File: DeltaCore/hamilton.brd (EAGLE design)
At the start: 45 x 41 mm, 68 parts, among them Q3 MOSFET-NCHANNEL_SOT23-3, Q4 MOSFET-NCHANNEL_SOT23-3, Q5 MOSFET-NCHANNEL_SOT23-3, Q6 MOSFET-NCHANNEL_SOT23-3, Q7 NFET_AON7408, Q8 NFET_AON7408, U1 SAMR21, U10 PCA9557, U2 APDS9007, U3 MMA7660FC, U4 AT30TS74, U5 MCP73871-2AAI/ML, U7 BQ29718, U8 MCP1824ST-3302E/DB, U9 TPS61090, X1 XTAL

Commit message: more
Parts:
- removed R3: 20k, storm:S0402
- removed U2: APDS9007, storm:APDS9007
- moved R14 1.16 mm to (26.7, 36.7), turned to 0 degrees
- moved C12 0.77 mm to (43.8, 18.9)
- moved R12 0.61 mm to (23.0, 39.0)
- moved C13 0.13 mm to (35.2, 39.7)
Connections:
- net +3V3: no longer U2.4, U5.17, U5.3, U5.4, U5.9
- net GND: no longer R3.P$1, U2.1
- net LS: no longer R3.P$2, U2.3
- net SD: no longer U2.6
- net VCC: now also U5.17, U5.3, U5.4, U5.9
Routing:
- net VCC: track 17.8 -> 41.8 mm, vias 0 -> 3
- net LS: track 22.3 -> 0.00 mm, vias 2 -> 0
- net +3V3: track 68.4 -> 52.8 mm, vias 13 -> 8
- net SD: track 13.9 -> 0.00 mm
- net SCL: track 52.8 -> 42.6 mm, vias 4 -> 2
- net GND: track 219.0 -> 209.5 mm, vias 60 -> 59
- net OUT: track 81.8 -> 83.6 mm
- net SDA: track 45.9 -> 47.5 mm
- net ACC: track 12.1 -> 10.8 mm, vias 1 -> 0
- net !RESET!: track 16.5 -> 17.8 mm
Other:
- board size 45 x 41 mm -> 45 x 41.5 mm

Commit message: add analog line for fan
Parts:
- added JP9: (no value), pinhead:1X01
- added R16: 5k, resistor:R0402
- added R3: 20k, resistor:R0402
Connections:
- new net N$8: JP9.1, R3.2
- new net N$9: R16.2, R3.1, U1.8
- net GND: now also R16.1
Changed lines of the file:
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@@
 <element name="R4" library="resistor" package="R0603" value="??" x="5.842" y="3.556" rot="R90"/>
 <element name="R15" library="resistor" package="R0603" value="??" x="8.382" y="3.556" rot="R270"/>
+<element name="JP9" library="pinhead" package="1X01" value="" x="7.112" y="10.922"/>
+<element name="R3" library="resistor" package="R0402" value="20k" x="0.254" y="-4.318"/>
+<element name="R16" library="resistor" package="R0402" value="5k" x="0.254" y="-7.874"/>
 </elements>
 <signals>
@@
 <wire x1="36.867" y1="30.912" x2="36.728" y2="31.051" width="0.1524" layer="1"/>
 <wire x1="36.728" y1="31.051" x2="36.347" y2="31.051" width="0.1524" layer="1"/>
+<contactref element="R16" pad="1"/>
+<wire x1="2.27" y1="4.556" x2="-0.396" y2="-7.874" width="0" layer="19" extent="1-1"/>
 </signal>
 <signal name="N$3">
@@
 <wire x1="41.159" y1="20.764" x2="39.8912" y2="20.764" width="0.1524" layer="1"/>
 <wire x1="36.708" y1="26.499" x2="36.708" y2="27.762" width="0.1524" layer="1"/>
-<wire x1="36.708" y1="26.499" x2="37.0078" y2="26.1992" width="0.1524" layer="1"/>
-<wire x1="37.0078" y1="26.1992" x2="37.0078" y2="22.4028" width="0.1524" layer="1"/>
+<wire x1="36.708" y1="26.499" x2="37.0078" y2="25.9452" width="0.1524" layer="1"/>
+<wire x1="37.0078" y1="25.9452" x2="37.0078" y2="22.4028" width="0.1524" layer="1"/>
 <wire x1="37.0078" y1="22.4028" x2="37.846" y2="22.4028" width="0.1524" layer="1"/>
 <wire x1="37.8714" y1="21.59" x2="39.1668" y2="21.59" width="0.1524" layer="1"/>
@@
 <wire x1="6.858" y1="8.116" x2="10.8864" y2="8.116" width="0.3048" layer="1"/>
 </signal>
+<signal name="N$8">
+<contactref element="JP9" pad="1"/>
+<contactref element="R3" pad="2"/>
+<wire x1="0.904" y1="-4.318" x2="7.112" y2="10.922" width="0" layer="19" extent="1-1"/>
+</signal>
+<signal name="N$9">
+<contactref element="R3" pad="1"/>
+<contactref element="R16" pad="2"/>
+<contactref element="U1" pad="8"/>
+<wire x1="-0.396" y1="-4.318" x2="37.208" y2="27.762" width="0" layer="19" extent="1-1"/>
+<wire x1="0.904" y1="-7.874" x2="-0.396" y2="-4.318" width="0" layer="19" extent="1-1"/>
+</signal>
 </signals>

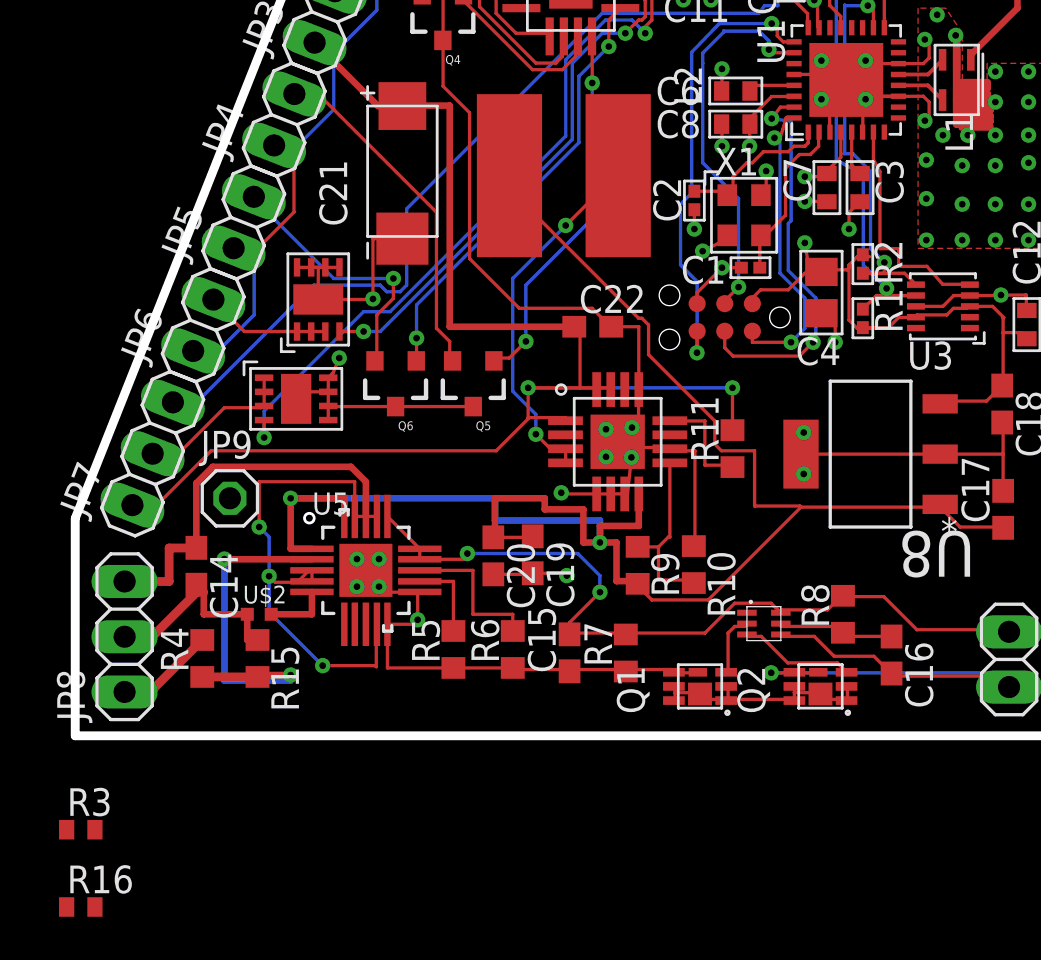
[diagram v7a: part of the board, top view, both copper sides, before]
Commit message: place resistors
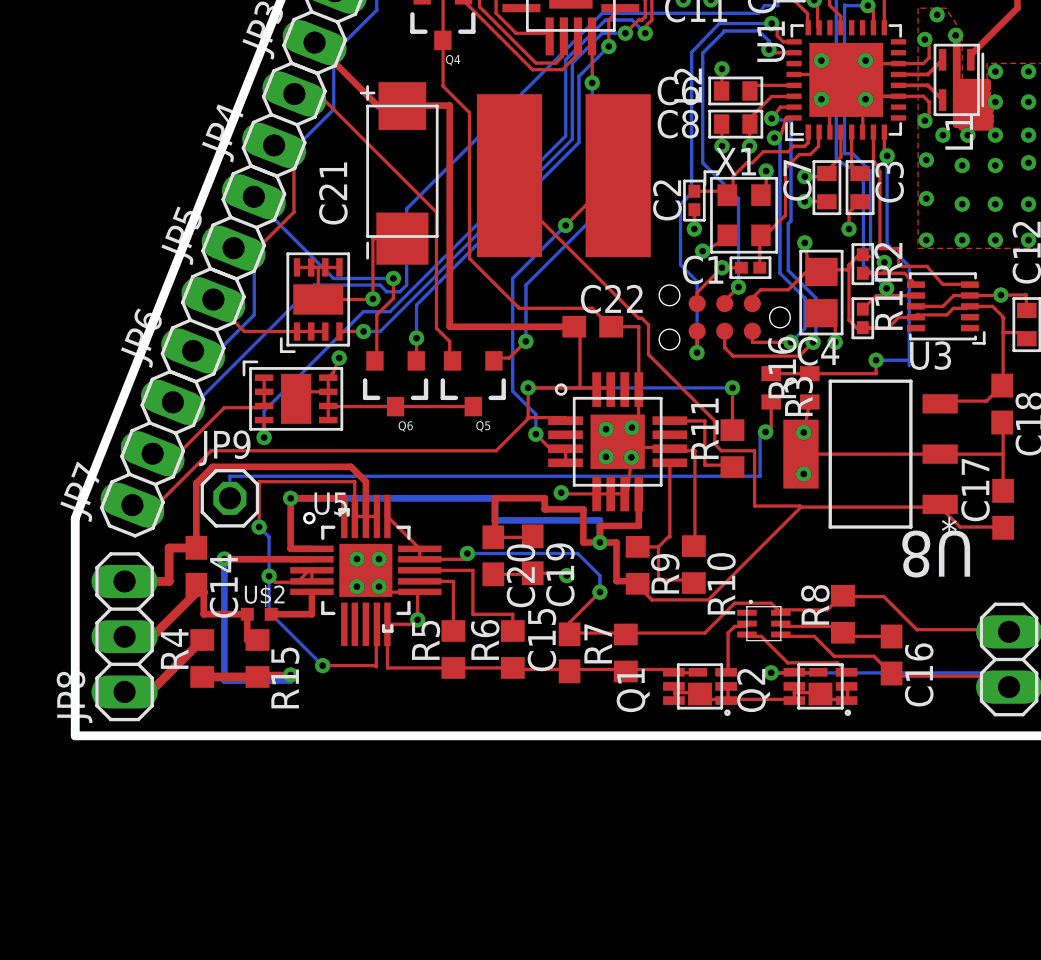
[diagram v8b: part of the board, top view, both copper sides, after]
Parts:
- moved R16 41.2 mm to (33.8, 16.0), turned to 90 degrees
- moved R3 37.7 mm to (32.0, 16.0), turned to 270 degrees
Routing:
- net N$8: track 0.00 -> 29.3 mm, vias 0 -> 1
- net N$9: track 0.00 -> 18.2 mm, vias 0 -> 2
- net GND: track 209.5 -> 210.9 mm
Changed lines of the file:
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@@
 <element name="R15" library="resistor" package="R0603" value="??" x="8.382" y="3.556" rot="R270"/>
 <element name="JP9" library="pinhead" package="1X01" value="" x="7.112" y="10.922"/>
-<element name="R3" library="resistor" package="R0402" value="20k" x="0.254" y="-4.318"/>
-<element name="R16" library="resistor" package="R0402" value="5k" x="0.254" y="-7.874"/>
+<element name="R3" library="resistor" package="R0402" value="20k" x="32.004" y="16.002" rot="R270"/>
+<element name="R16" library="resistor" package="R0402" value="5k" x="33.782" y="16.002" rot="R90"/>
 </elements>
 <signals>
@@
 <wire x1="36.728" y1="31.051" x2="36.347" y2="31.051" width="0.1524" layer="1"/>
 <contactref element="R16" pad="1"/>
-<wire x1="2.27" y1="4.556" x2="-0.396" y2="-7.874" width="0" layer="19" extent="1-1"/>
+<wire x1="33.782" y1="15.352" x2="33.5026" y2="13.9446" width="0.1524" layer="1"/>
 </signal>
 <signal name="N$3">
@@
 <contactref element="JP9" pad="1"/>
 <contactref element="R3" pad="2"/>
-<wire x1="0.904" y1="-4.318" x2="7.112" y2="10.922" width="0" layer="19" extent="1-1"/>
+<wire x1="32.004" y1="15.352" x2="32.004" y2="13.97" width="0.1524" layer="1"/>
+<wire x1="32.004" y1="13.97" x2="31.75" y2="13.97" width="0.1524" layer="1"/>
+<via x="31.75" y="13.97" extent="1-16" drill="0.3048"/>
+<wire x1="31.75" y1="13.97" x2="31.496" y2="13.97" width="0.1524" layer="16"/>
+<wire x1="31.496" y1="13.97" x2="31.496" y2="11.938" width="0.1524" layer="16"/>
+<wire x1="31.496" y1="11.938" x2="7.112" y2="11.938" width="0.1524" layer="16"/>
+<wire x1="7.112" y1="11.938" x2="7.112" y2="10.922" width="0.1524" layer="16"/>
 </signal>
 <signal name="N$9">
@@
 <contactref element="R16" pad="2"/>
 <contactref element="U1" pad="8"/>
-<wire x1="-0.396" y1="-4.318" x2="37.208" y2="27.762" width="0" layer="19" extent="1-1"/>
-<wire x1="0.904" y1="-7.874" x2="-0.396" y2="-4.318" width="0" layer="19" extent="1-1"/>
+<wire x1="37.208" y1="27.762" x2="37.208" y2="26.8" width="0.1524" layer="1"/>
+<wire x1="37.208" y1="26.8" x2="37.338" y2="26.67" width="0.1524" layer="1"/>
+<via x="37.338" y="26.67" extent="1-16" drill="0.3048"/>
+<wire x1="37.338" y1="26.67" x2="37.338" y2="22.606" width="0.1524" layer="16"/>
+<wire x1="37.338" y1="22.606" x2="38.354" y2="21.59" width="0.1524" layer="16"/>
+<wire x1="38.354" y1="21.59" x2="38.354" y2="17.272" width="0.1524" layer="16"/>
+<wire x1="38.354" y1="17.272" x2="38.354" y2="17.018" width="0.1524" layer="16"/>
+<wire x1="32.004" y1="16.652" x2="33.782" y2="16.652" width="0.1524" layer="1"/>
+<wire x1="33.782" y1="16.652" x2="36.83" y2="16.652" width="0.1524" layer="1"/>
+<wire x1="36.83" y1="16.652" x2="36.83" y2="17.272" width="0.1524" layer="1"/>
+<via x="36.83" y="17.272" extent="1-16" drill="0.3048"/>
+<wire x1="36.83" y1="17.272" x2="38.354" y2="17.272" width="0.1524" layer="16"/>
 </signal>
 </signals>
